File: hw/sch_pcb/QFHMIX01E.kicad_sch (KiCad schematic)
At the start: 81 parts, among them J1 HEADER_1x08, M1 HOLE, M2 HOLE, M3 HOLE, M4 HOLE, M5 HOLE, M6 HOLE, M7 HOLE, M8 HOLE, U1 Si53322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

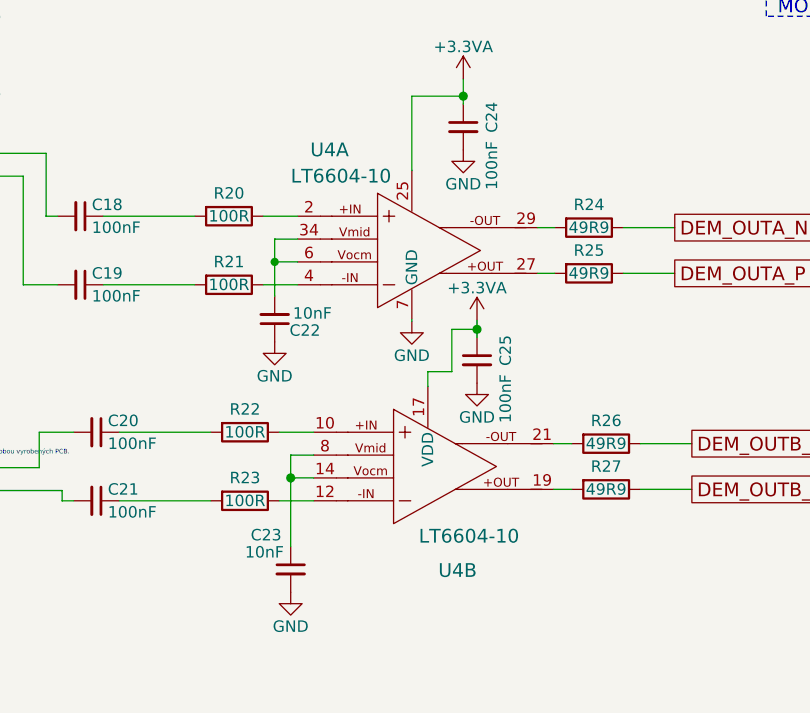
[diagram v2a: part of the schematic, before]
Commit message: Update LT6604 to 5MHz bandwidth variant.
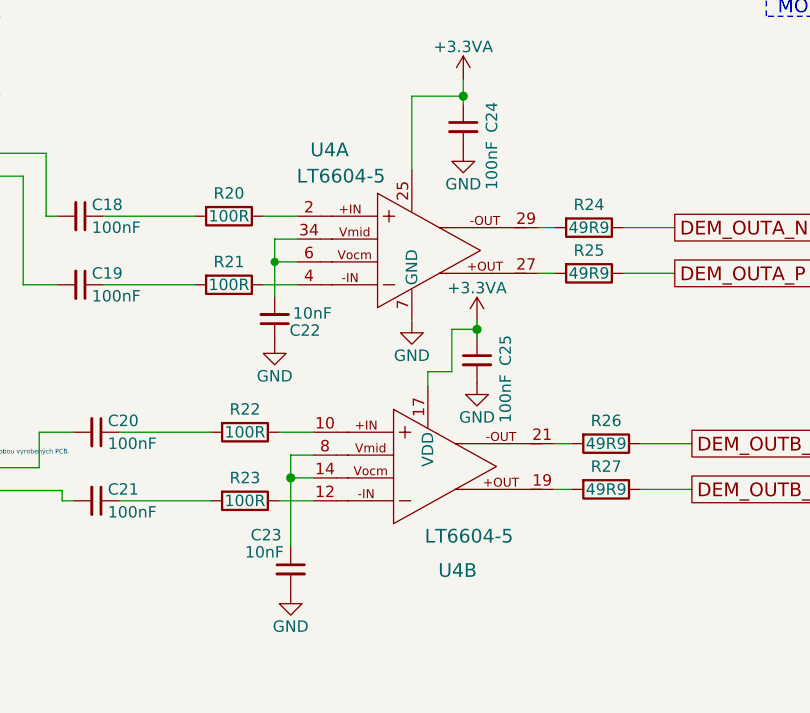
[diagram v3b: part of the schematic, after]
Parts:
- U4: value LT6604-10 -> LT6604-5
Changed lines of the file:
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@@
       (effects (font (size 1.524 1.524)))
     )
-    (property "Value" "LT6604-10" (id 1) (at 210.566 67.945 0)
+    (property "Value" "LT6604-5" (id 1) (at 210.566 67.945 0)
       (effects (font (size 1.524 1.524)))
     )
@@
       (effects (font (size 1.524 1.524)) hide)
     )
-    (property "Datasheet" "https://www.analog.com/media/en/technical-documentation/data-sheets/660410fb.pdf" (id 3) (at 187.96 67.31 0)
+    (property "Datasheet" "https://www.analog.com/media/en/technical-documentation/data-sheets/66045fa.pdf" (id 3) (at 187.96 67.31 0)
       (effects (font (size 1.524 1.524)) hide)
     )
@@
       (effects (font (size 1.524 1.524)))
     )
-    (property "Value" "LT6604-10" (id 1) (at 224.79 107.95 0)
+    (property "Value" "LT6604-5" (id 1) (at 224.79 107.95 0)
       (effects (font (size 1.524 1.524)))
     )
@@
       (effects (font (size 1.524 1.524)) hide)
     )
-    (property "Datasheet" "https://www.analog.com/media/en/technical-documentation/data-sheets/660410fb.pdf" (id 3) (at 189.738 91.313 0)
+    (property "Datasheet" "https://www.analog.com/media/en/technical-documentation/data-sheets/66045fa.pdf" (id 3) (at 189.738 91.313 0)
       (effects (font (size 1.524 1.524)) hide)
     )
@@
     )
     (path "/bef43be7-ca72-4d07-996b-877c1990a309"
-      (reference "U4") (unit 1) (value "LT6604-10") (footprint "Mlab_IO:UFF_QFN34")
+      (reference "U4") (unit 1) (value "LT6604-5") (footprint "Mlab_IO:UFF_QFN34")
     )
     (path "/d5a1c65c-50ea-4b5b-b77d-734a379bde8b"
-      (reference "U4") (unit 2) (value "LT6604-10") (footprint "Mlab_IO:UFF_QFN34")
+      (reference "U4") (unit 2) (value "LT6604-5") (footprint "Mlab_IO:UFF_QFN34")
     )
     (path "/00000000-0000-0000-0000-00005ccb1e0f/883127bd-d13a-43c5-b13d-fc41cb89b718"

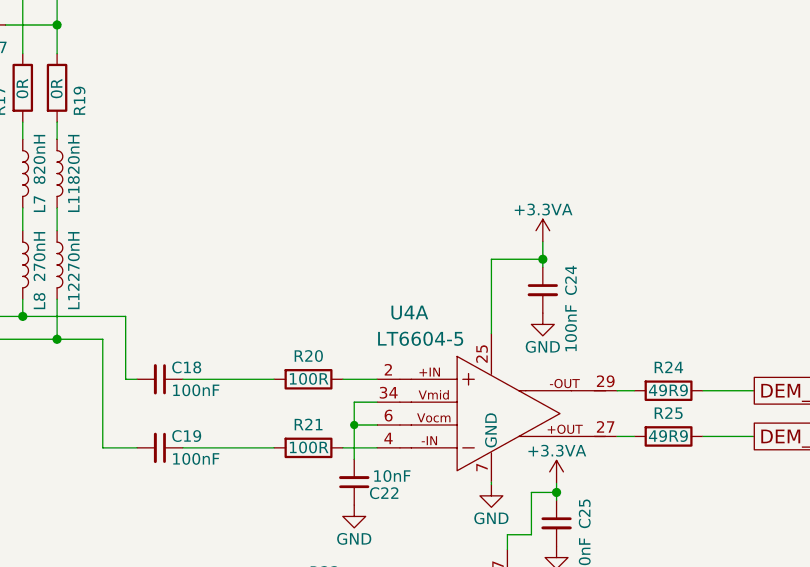
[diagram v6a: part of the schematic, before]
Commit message: Add note about gain settings to schematics.
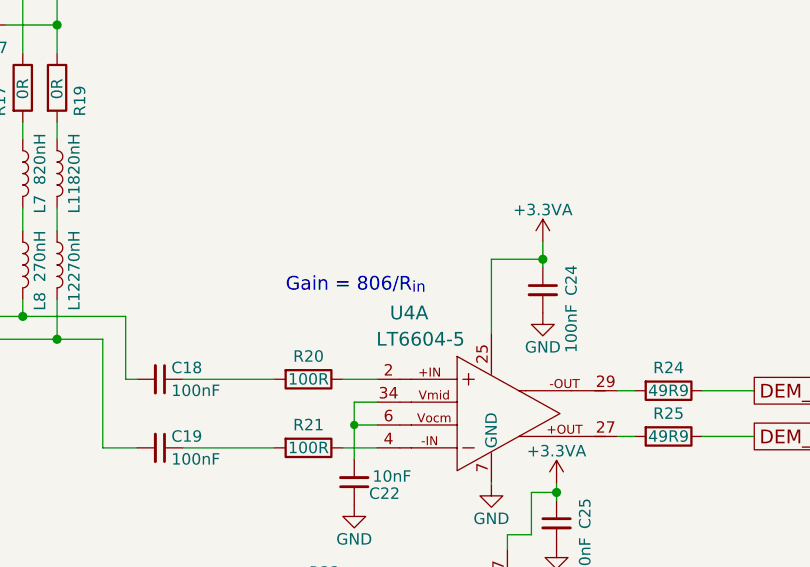
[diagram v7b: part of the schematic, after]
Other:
- note added: "Gain = 806/R_{in}"
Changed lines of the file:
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@@
+    (effects (font (size 1.524 1.524)) (justify left bottom))
+  )
+  (text "Gain = 806/R_{in}" (at 195.58 62.865 0)
     (effects (font (size 1.524 1.524)) (justify left bottom))
   )
